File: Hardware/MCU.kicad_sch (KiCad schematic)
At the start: 37 parts, among them J5 Conn_01x05_Pin, Q1 BC847, SW1 SW_Push, SW2 SW_SPDT, U1 STM32F405RGT6, Y2 25MHz

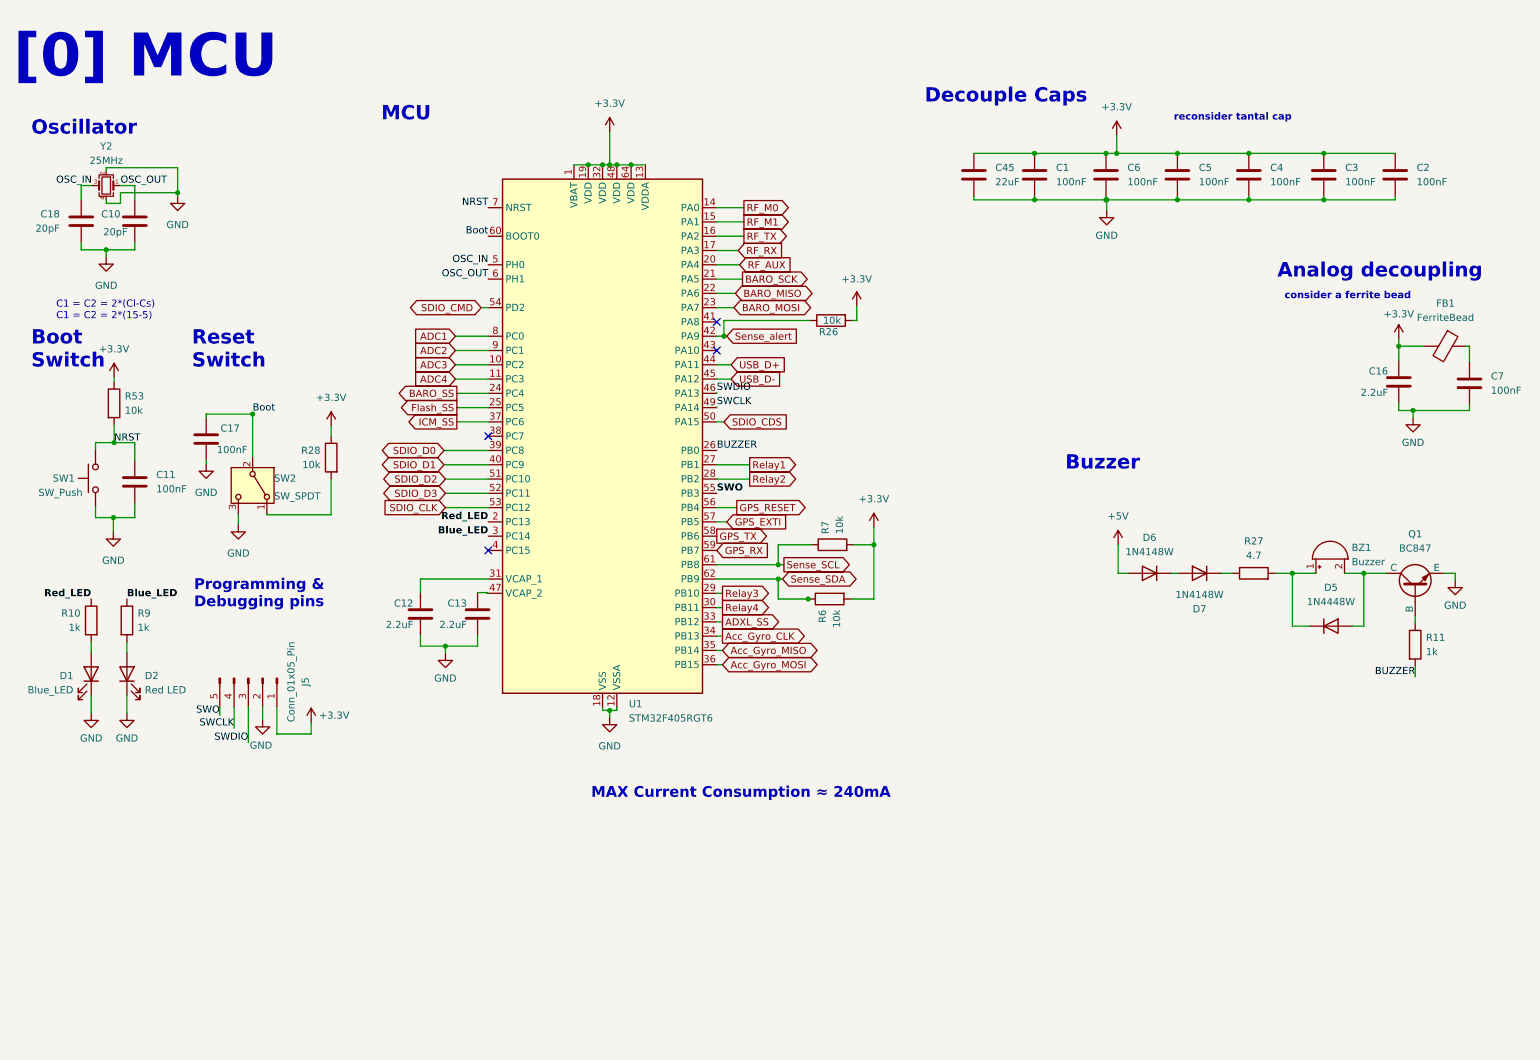
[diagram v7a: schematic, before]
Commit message: Added New file for additional resources used, Changed LDO for lower noise, changed buck converter for higher switching speed, smaller inductance value, better transient current response
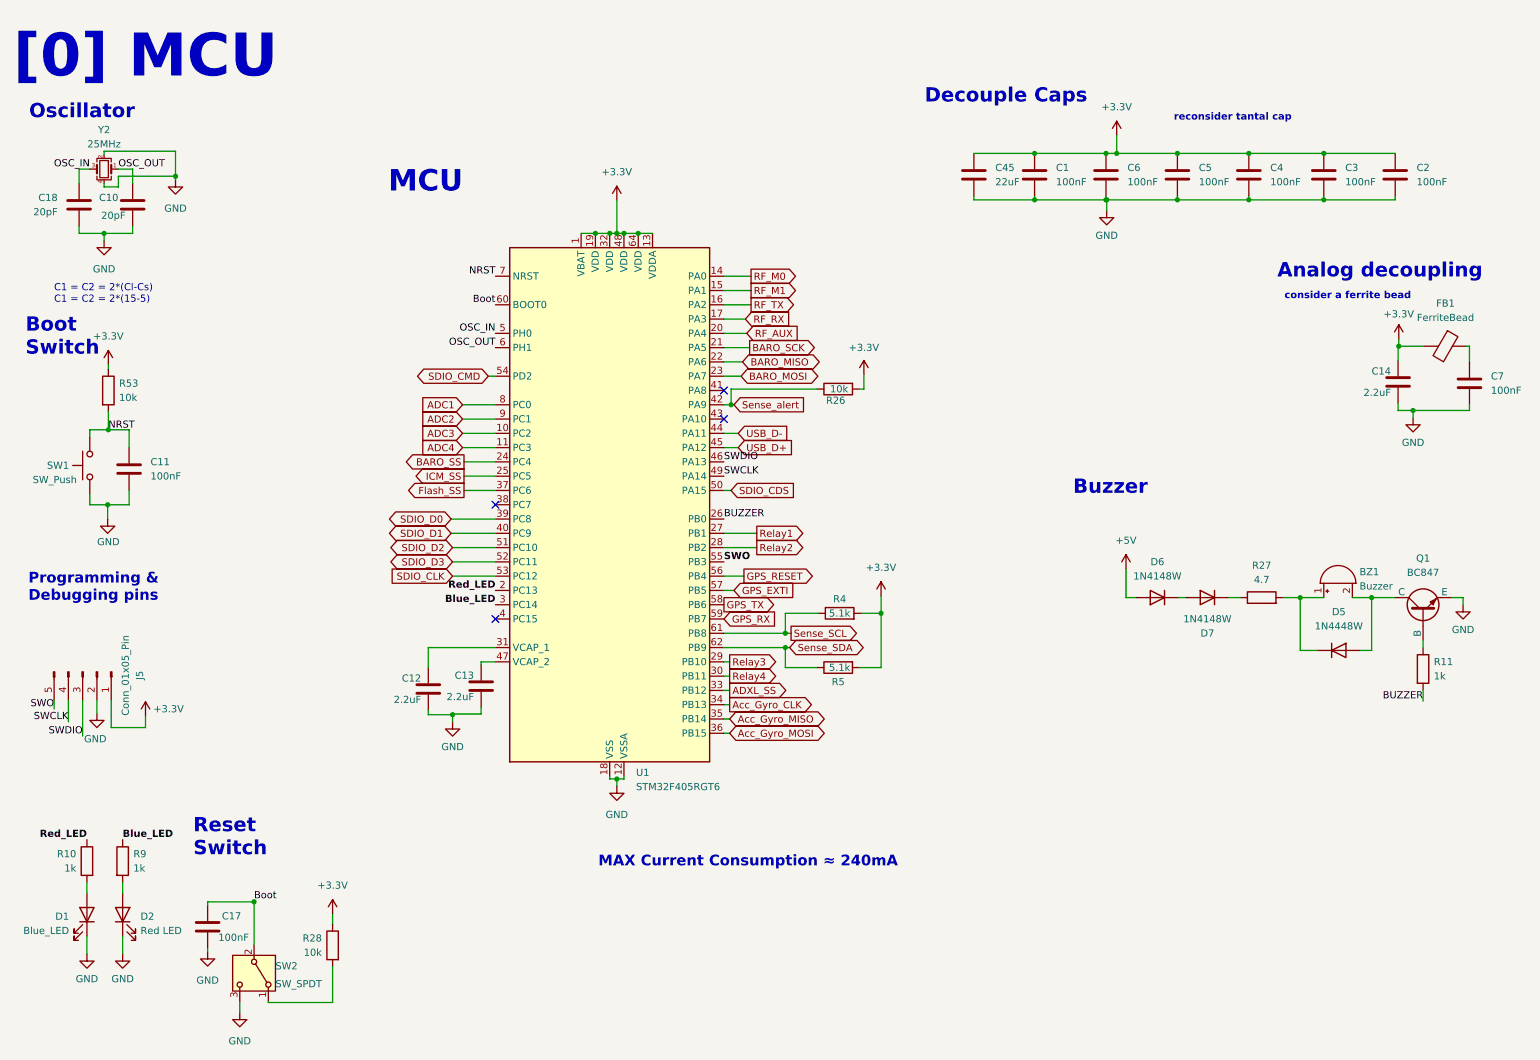
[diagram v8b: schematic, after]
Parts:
- removed C16: 2.2uF, Capacitor_SMD:C_0402_1005Metric, symbol Device:C
- removed R6, R7: 10k, Resistor_SMD:R_0402_1005Metric, symbol Device:R
- added C14: 2.2uF, Capacitor_SMD:C_0603_1608Metric, symbol Device:C
- added R4, R5: 5.1k, Resistor_SMD:R_0402_1005Metric, symbol Device:R
- C12, C13: footprint Capacitor_SMD:C_0402_1005Metric -> Capacitor_SMD:C_0603_1608Metric; Distributer Link http://ozdisan.com/p/smt-smd-ve-mlcc-kapasitorler-184/murat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 -> https://www.ozdisan.com/p/smt-smd-ve-mlcc-kapasitorler-184/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; Part Number GRT155C81A225ME13D -> CL10B225KP8NNNC
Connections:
- net +3.3V: now also C14.1, R4.2, R5.2
- net Flash_SS: now also U1.37 (PC6); no longer U1.25 (PC5)
- net GND: now also C14.2
- net ICM_SS: now also U1.25 (PC5); no longer U1.37 (PC6)
- net Sense_SCL: now also R4.1
- net Sense_SDA: now also R5.1
- net USB_D+: now also U1.45 (PA12); no longer U1.44 (PA11)
- net USB_D-: now also U1.44 (PA11); no longer U1.45 (PA12)
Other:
- moved on the sheet: BZ1, C10, C11, C12, C17, C18, D1, D2, D5, D6, D7, J5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
